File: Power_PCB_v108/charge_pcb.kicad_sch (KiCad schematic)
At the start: 42 parts, among them J1 Mow3, J10 Mot_Left, J11 DC/DC1, J12 DC/DC2, J2 Main_PCB1, J3 Mow2, J4 Battery, J5 Main_PCB2, J6 Power Switch, J7 Mow1, J8 Mot_Right, J9 Start, Q1 BC547C, Q2 IRF9540N, Q3 BC547C, Q4 IRF9540N, U1 INA226, U2 INA226, U3 INA226, U4 INA226, U5 INA226, U6 INA226

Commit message: Change Diode
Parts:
- removed D3, D5: SB1240, Diode_THT:D_DO-41_SOD81_P10.16mm_Horizontal, symbol charge_pcb-rescue:DIODE-Lötpad_2,5mm-charge_pcb-rescue
- added D3, D5: SB1240, Diode_THT:D_DO-41_SOD81_P10.16mm_Horizontal, symbol Diode:1N5401
- added JP1: Jumper Charge, Connector_PinHeader_2.54mm:PinHeader_1x02_P2.54mm_Vertical, symbol Device:Jumper
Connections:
- net at D1.1 (K), F1.2, R1.1: now also D3.2 (A)
- net at Q2.3 (S), R4.1: now also D3.1 (K), JP1.1
- net at J4.1, J6.1, U3.10 (IN1-): now also JP1.2
- net at D4.1 (K), F2.2: now also D5.2 (A)
- net at Q4.3 (S), R7.1: now also D5.1 (K)

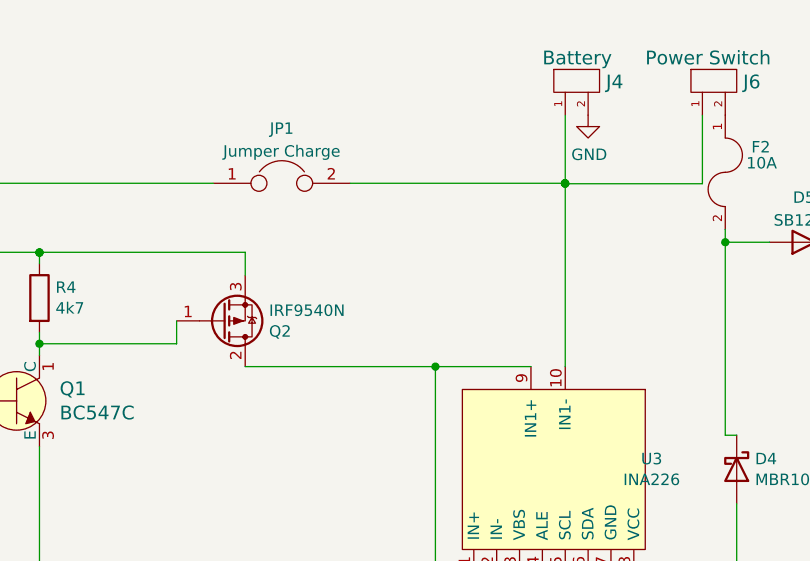
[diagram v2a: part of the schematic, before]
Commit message: Connection from jumper changed
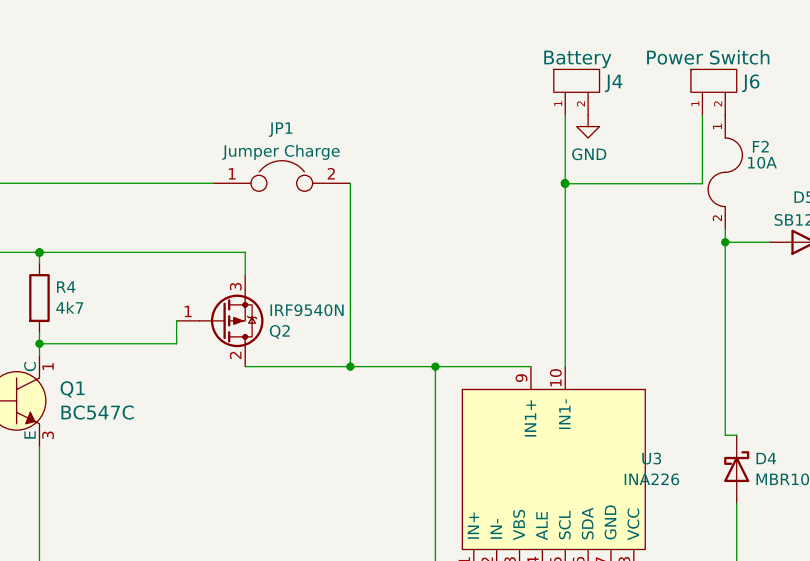
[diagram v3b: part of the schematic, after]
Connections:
- net at J4.1, J6.1, U3.10 (IN1-): no longer JP1.2
- net at Q2.2 (D), U3.3 (VBS), U3.9 (IN1+): now also JP1.2
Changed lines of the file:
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@@
   (junction (at 243.84 40.5892) (diameter 0) (color 0 0 0 0)
+  )
+  (junction (at 122.174 49.53) (diameter 0) (color 0 0 0 0)
   )
   (junction (at 200.66 59.055) (diameter 0) (color 0 0 0 0)
@@
     (stroke (width 0) (type default) (color 0 0 0 0))
   )
+  (wire (pts (xy 122.174 29.1592) (xy 122.174 49.53))
+    (stroke (width 0) (type default) (color 0 0 0 0))
+  )
   (wire (pts (xy 15.24 36.83) (xy 25.4 36.83))
     (stroke (width 0) (type default) (color 0 0 0 0))
@@
     (stroke (width 0) (type default) (color 0 0 0 0))
   )
-  (wire (pts (xy 110.49 49.53) (xy 131.6228 49.53))
+  (wire (pts (xy 110.49 49.53) (xy 122.174 49.53))
     (stroke (width 0) (type default) (color 0 0 0 0))
   )
@@
     (stroke (width 0) (type default) (color 0 0 0 0))
   )
+  (wire (pts (xy 122.174 49.53) (xy 131.6228 49.53))
+    (stroke (width 0) (type default) (color 0 0 0 0))
+  )
   (wire (pts (xy 76.2 127) (xy 78.74 127))
     (stroke (width 0) (type default) (color 0 0 0 0))
@@
     (stroke (width 0) (type default) (color 0 0 0 0))
   )
-  (wire (pts (xy 122.174 29.1592) (xy 145.9992 29.1592))
-    (stroke (width 0) (type default) (color 0 0 0 0))
-  )

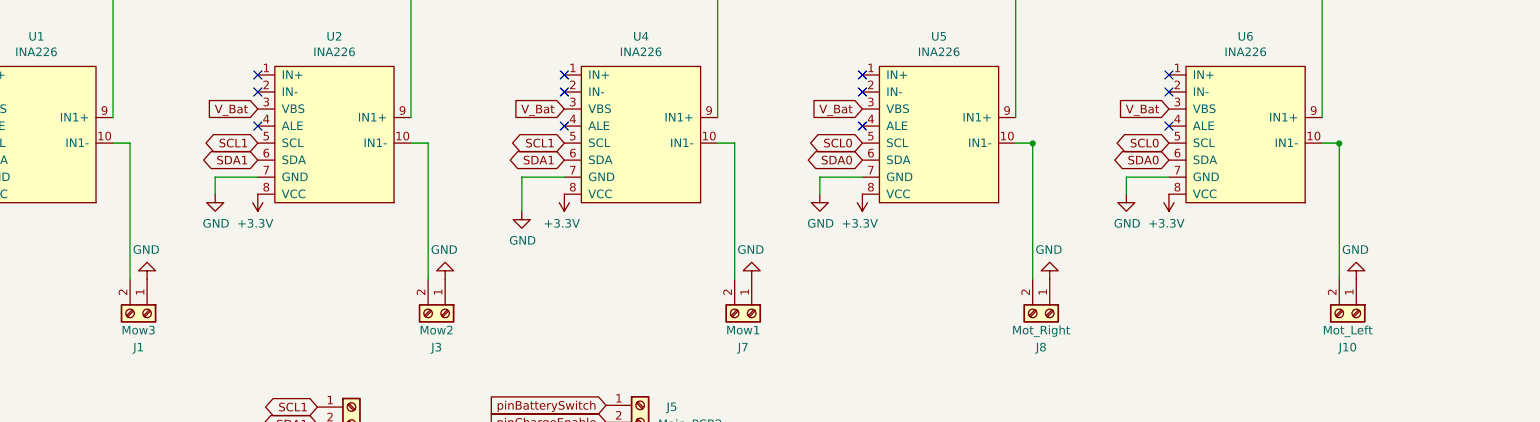
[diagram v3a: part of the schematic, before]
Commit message: Add MBR1045
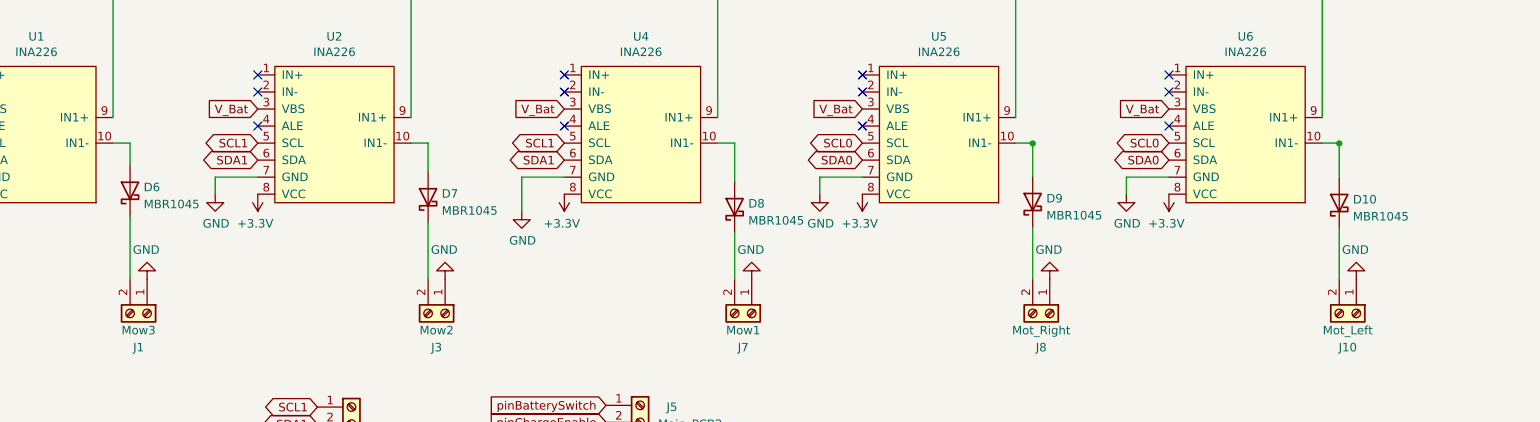
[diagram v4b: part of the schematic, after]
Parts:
- added D10, D6, D7, D8, D9: MBR1045, Package_TO_SOT_THT:TO-220-2_Vertical, symbol Diode:MBR735
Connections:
- net at U6.10 (IN1-): now also D10.2 (A); no longer J10.2 (Pin_2)
- net at U5.10 (IN1-): now also D9.2 (A); no longer J8.2 (Pin_2)
- net at U4.10 (IN1-): now also D8.2 (A); no longer J7.2 (Pin_2)
- net at U2.10 (IN1-): now also D7.2 (A); no longer J3.2 (Pin_2)
- net at U1.10 (IN1-): now also D6.2 (A); no longer J1.2 (Pin_2)
- new net: D10.1 (K), J10.2 (Pin_2)
- new net: D9.1 (K), J8.2 (Pin_2)
- new net: D8.1 (K), J7.2 (Pin_2)
- new net: D7.1 (K), J3.2 (Pin_2)
- new net: D6.1 (K), J1.2 (Pin_2)
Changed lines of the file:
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@@
+    (stroke (width 0) (type default) (color 0 0 0 0))
+  )
+  (wire (pts (xy 123.19 138.8872) (xy 123.19 147.32))
     (stroke (width 0) (type default) (color 0 0 0 0))
   )
@@
     (stroke (width 0) (type default) (color 0 0 0 0))
   )
+  (wire (pts (xy 78.74 137.922) (xy 78.74 147.32))
+    (stroke (width 0) (type default) (color 0 0 0 0))
+  )
   (wire (pts (xy 97.79 132.08) (xy 91.44 132.08))
     (stroke (width 0) (type default) (color 0 0 0 0))
@@
     (stroke (width 0) (type default) (color 0 0 0 0))
   )
-  (wire (pts (xy 213.36 127.0508) (xy 213.36 147.32))
+  (wire (pts (xy 213.36 127.0508) (xy 213.36 131.9784))
     (stroke (width 0) (type default) (color 0 0 0 0))
   )
@@
     (stroke (width 0) (type default) (color 0 0 0 0))
   )
+  (wire (pts (xy 259.08 139.7508) (xy 259.08 147.32))
+    (stroke (width 0) (type default) (color 0 0 0 0))
+  )
   (wire (pts (xy 50.8 73.66) (xy 66.421 73.66))
     (stroke (width 0) (type default) (color 0 0 0 0))
   )
-  (wire (pts (xy 168.91 127) (xy 168.91 147.32))
+  (wire (pts (xy 168.91 127) (xy 168.91 132.7404))
     (stroke (width 0) (type default) (color 0 0 0 0))
   )
@@
     (stroke (width 0) (type default) (color 0 0 0 0))
   )
-  (wire (pts (xy 78.74 127) (xy 78.74 147.32))
+  (wire (pts (xy 78.74 127) (xy 78.74 130.302))
     (stroke (width 0) (type default) (color 0 0 0 0))
   )
@@
     (stroke (width 0) (type default) (color 0 0 0 0))
   )
-  (wire (pts (xy 123.19 127) (xy 123.19 147.32))
+  (wire (pts (xy 123.19 127) (xy 123.19 131.2672))
     (stroke (width 0) (type default) (color 0 0 0 0))
   )
@@
     (stroke (width 0) (type default) (color 0 0 0 0))
   )
-  (wire (pts (xy 259.08 127.0508) (xy 259.08 147.32))
+  (wire (pts (xy 259.08 127.0508) (xy 259.08 132.1308))
     (stroke (width 0) (type default) (color 0 0 0 0))
   )
@@
     (stroke (width 0) (type default) (color 0 0 0 0))
   )
+  (wire (pts (xy 168.91 140.3604) (xy 168.91 147.32))
+    (stroke (width 0) (type default) (color 0 0 0 0))
+  )
   (wire (pts (xy 243.8908 50.8) (xy 243.8908 97.282))
     (stroke (width 0) (type default) (color 0 0 0 0))
@@
   )
   (wire (pts (xy 176.3776 35.7124) (xy 177.8 35.7124))
+    (stroke (width 0) (type default) (color 0 0 0 0))
+  )
+  (wire (pts (xy 213.36 139.5984) (xy 213.36 147.32))
     (stroke (width 0) (type default) (color 0 0 0 0))
   )
@@
     (pin "2")
   )
+  (symbol (lib_id "Diode:MBR735") (at 168.91 136.5504 90) (unit 1)
+    (in_bom yes) (on_board yes) (fields_autoplaced)
+    (property "Reference" "D8" (id 0) (at 170.942 136.0332 90)
+      (effects (font (size 1.27 1.27)) (justify right))
+    )
+    (property "Value" "MBR1045" (id 1) (at 170.942 138.5701 90)
+      (effects (font (size 1.27 1.27)) (justify right))
+    )
+    (property "Footprint" "Package_TO_SOT_THT:TO-220-2_Vertical" (id 2) (at 173.355 136.5504 0)
+      (effects (font (size 1.27 1.27)) hide)
+    )
+    (property "Datasheet" "http://www.onsemi.com/pub_link/Collateral/MBR735-D.PDF" (id 3) (at 168.91 136.5504 0)
+      (effects (font (size 1.27 1.27)) hide)
+    )
+    (pin "1")
+    (pin "2")
+  )
   (symbol (lib_id "power:GND") (at 15.24 73.66 0) (unit 1)
     (in_bom yes) (on_board yes)
@@
     )
     (pin "1")
+  )
+  (symbol (lib_id "Diode:MBR735") (at 213.36 135.7884 90) (unit 1)
+    (in_bom yes) (on_board yes) (fields_autoplaced)
+    (property "Reference" "D9" (id 0) (at 215.392 135.2712 90)
+      (effects (font (size 1.27 1.27)) (justify right))
+    )
+    (property "Value" "MBR1045" (id 1) (at 215.392 137.8081 90)
+      (effects (font (size 1.27 1.27)) (justify right))
+    )
+    (property "Footprint" "Package_TO_SOT_THT:TO-220-2_Vertical" (id 2) (at 217.805 135.7884 0)
+      (effects (font (size 1.27 1.27)) hide)
+    )
+    (property "Datasheet" "http://www.onsemi.com/pub_link/Collateral/MBR735-D.PDF" (id 3) (at 213.36 135.7884 0)
+      (effects (font (size 1.27 1.27)) hide)
+    )
+    (pin "1")
+    (pin "2")
+  )
+  (symbol (lib_id "Diode:MBR735") (at 259.08 135.9408 90) (unit 1)
+    (in_bom yes) (on_board yes) (fields_autoplaced)
+    (property "Reference" "D10" (id 0) (at 261.112 135.4236 90)
+      (effects (font (size 1.27 1.27)) (justify right))
+    )
+    (property "Value" "MBR1045" (id 1) (at 261.112 137.9605 90)
+      (effects (font (size 1.27 1.27)) (justify right))
+    )
+    (property "Footprint" "Package_TO_SOT_THT:TO-220-2_Vertical" (id 2) (at 263.525 135.9408 0)
+      (effects (font (size 1.27 1.27)) hide)
+    )
+    (property "Datasheet" "http://www.onsemi.com/pub_link/Collateral/MBR735-D.PDF" (id 3) (at 259.08 135.9408 0)
+      (effects (font (size 1.27 1.27)) hide)
+    )
+    (pin "1")
+    (pin "2")
+  )
+  (symbol (lib_id "Diode:MBR735") (at 123.19 135.0772 90) (unit 1)
+    (in_bom yes) (on_board yes) (fields_autoplaced)
+    (property "Reference" "D7" (id 0) (at 125.222 134.56 90)
+      (effects (font (size 1.27 1.27)) (justify right))
+    )
+    (property "Value" "MBR1045" (id 1) (at 125.222 137.0969 90)
+      (effects (font (size 1.27 1.27)) (justify right))
+    )
+    (property "Footprint" "Package_TO_SOT_THT:TO-220-2_Vertical" (id 2) (at 127.635 135.0772 0)
+      (effects (font (size 1.27 1.27)) hide)
+    )
+    (property "Datasheet" "http://www.onsemi.com/pub_link/Collateral/MBR735-D.PDF" (id 3) (at 123.19 135.0772 0)
+      (effects (font (size 1.27 1.27)) hide)
+    )
+    (pin "1")
+    (pin "2")
   )
   (symbol (lib_id "power:GND") (at 239.6236 73.66 0) (unit 1)
@@
     (pin "1")
   )
+  (symbol (lib_id "Diode:MBR735") (at 78.74 134.112 90) (unit 1)
+    (in_bom yes) (on_board yes) (fields_autoplaced)
+    (property "Reference" "D6" (id 0) (at 80.772 133.5948 90)
+      (effects (font (size 1.27 1.27)) (justify right))
+    )
+    (property "Value" "MBR1045" (id 1) (at 80.772 136.1317 90)
+      (effects (font (size 1.27 1.27)) (justify right))
+    )
+    (property "Footprint" "Package_TO_SOT_THT:TO-220-2_Vertical" (id 2) (at 83.185 134.112 0)
+      (effects (font (size 1.27 1.27)) hide)
+    )
+    (property "Datasheet" "http://www.onsemi.com/pub_link/Collateral/MBR735-D.PDF" (id 3) (at 78.74 134.112 0)
+      (effects (font (size 1.27 1.27)) hide)
+    )
+    (pin "1")
+    (pin "2")
+  )
   (sheet_instances
     (path "/" (page "1"))
@@
       (reference "D5") (unit 1) (value "SB1240") (footprint "Diode_THT:D_DO-41_SOD81_P10.16mm_Horizontal")
     )
+    (path "/fb8819da-7e36-4f2d-9513-d3ee2c37acd3"
+      (reference "D6") (unit 1) (value "MBR1045") (footprint "Package_TO_SOT_THT:TO-220-2_Vertical")
+    )
+    (path "/6be5fe78-49f7-4ee1-b805-e55867aaa4e7"
+      (reference "D7") (unit 1) (value "MBR1045") (footprint "Package_TO_SOT_THT:TO-220-2_Vertical")
+    )
+    (path "/10bcfbba-d01a-41bf-8f33-a047b338fd13"
+      (reference "D8") (unit 1) (value "MBR1045") (footprint "Package_TO_SOT_THT:TO-220-2_Vertical")
+    )
+    (path "/48a788a6-03a1-4dbe-b953-00153c258d6d"
+      (reference "D9") (unit 1) (value "MBR1045") (footprint "Package_TO_SOT_THT:TO-220-2_Vertical")
+    )
+    (path "/6804103c-e79e-4bc9-afe2-ae94c052667e"
+      (reference "D10") (unit 1) (value "MBR1045") (footprint "Package_TO_SOT_THT:TO-220-2_Vertical")
+    )
     (path "/00000000-0000-0000-0000-000060704371"
